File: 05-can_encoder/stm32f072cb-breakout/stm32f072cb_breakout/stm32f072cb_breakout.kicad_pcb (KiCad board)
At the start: 2 copper layers, 25 x 25 mm, 11 parts, among them IC1 STM32F072CBT6, J1 Conn_01x08, J2 Conn_01x08

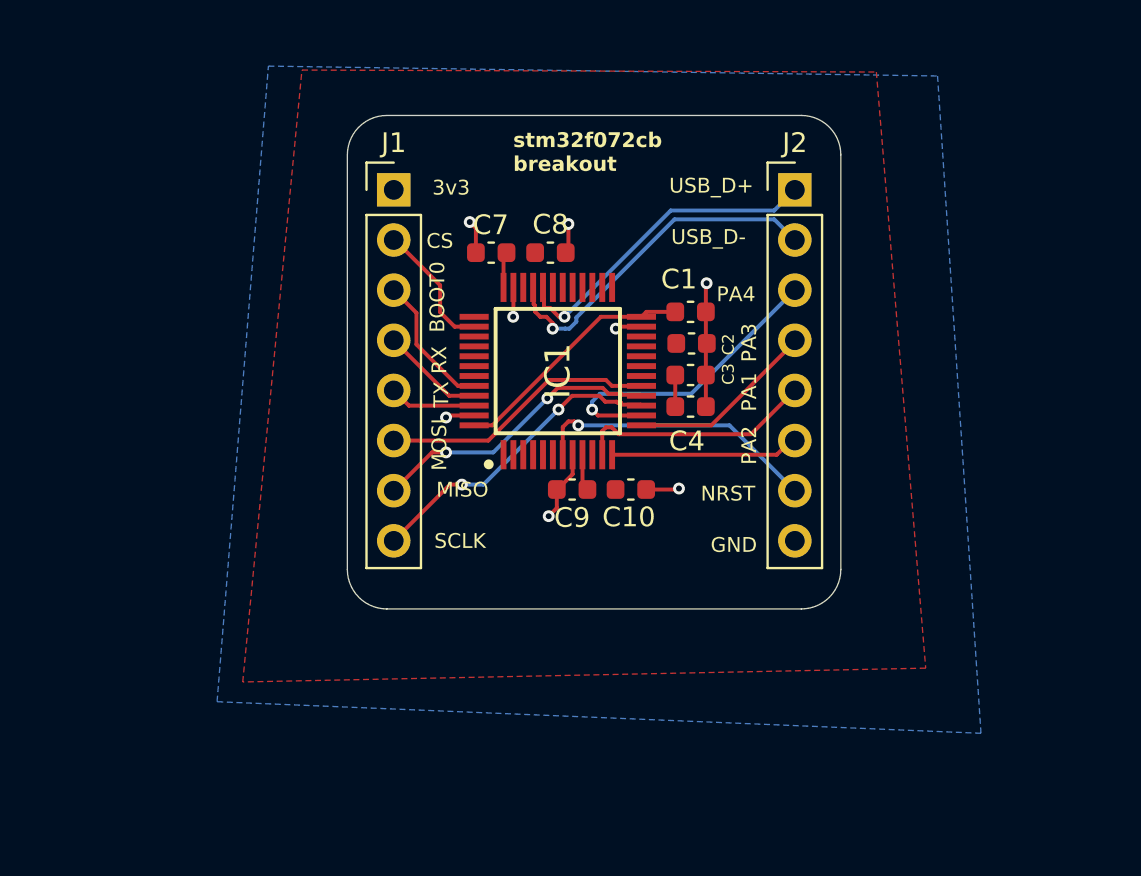
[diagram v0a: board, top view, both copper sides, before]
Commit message: stm and encoder breakout done/ordered
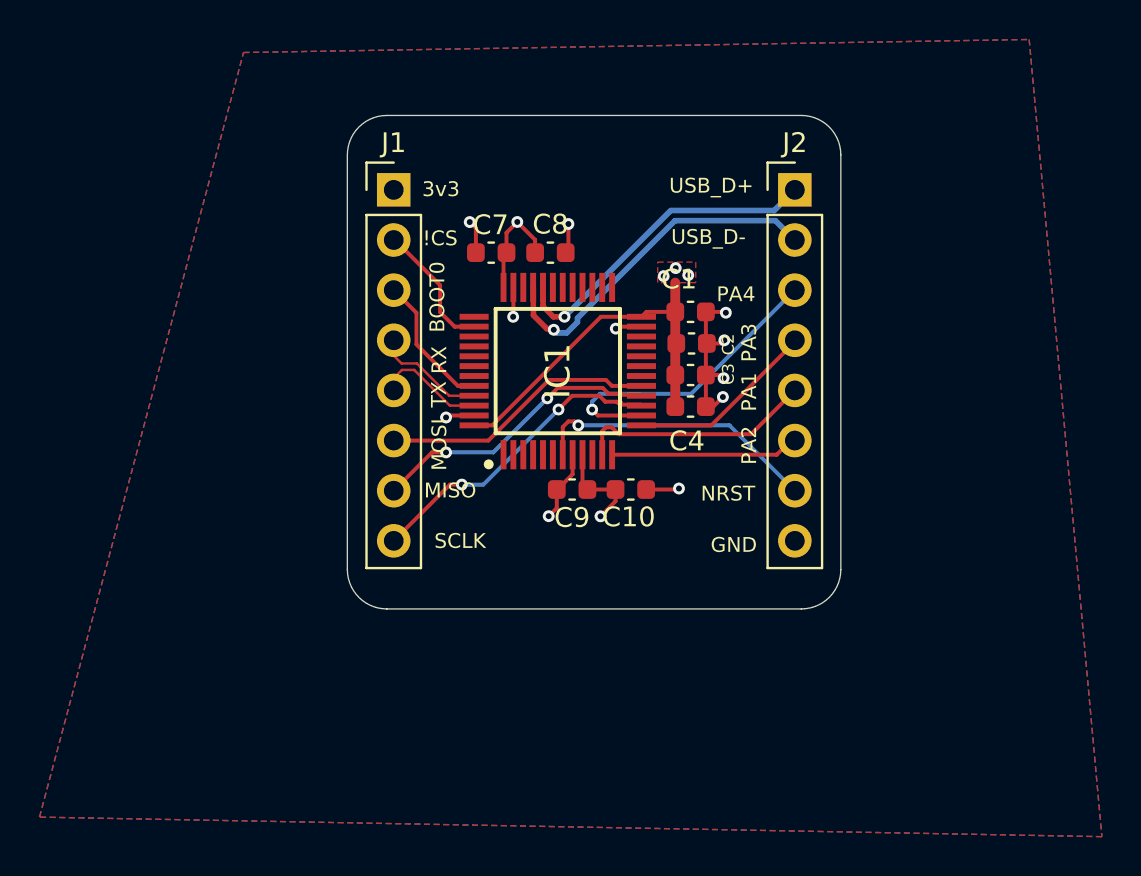
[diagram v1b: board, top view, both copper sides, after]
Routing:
- net 3v3: track 17.9 -> 29.3 mm, vias 0 -> 5
- net GND: track 19.1 -> 21.6 mm, vias 8 -> 11
- net can_tx: track 4.39 -> 5.62 mm
- added copper zone on B.Cu, net (none)
- added copper zone on F.Cu, net (none)
- added copper zone on In2.Cu, net 3v3
- added copper zone on In1.Cu, net GND
- removed copper zone on B.Cu, net GND
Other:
- copper layers 2 -> 4
- board text added: "!CS"
- board text added: "BJR@JHU STM32F072CB Breakout 22XT Cyan Brown"
- board text removed: "CS"
- board text removed: "stm32f072cb breakout"
